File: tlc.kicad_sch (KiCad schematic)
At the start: 13 parts, among them U2 TL074, U3 TL074, U4 TLC7528

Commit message: started to work on power part
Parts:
- renumbered C1 to C7, C2 to C8, R1 to R19, R2 to R20, R3 to R21, R4 to R22, R5 to R23, R6 to R24, R7 to R25, R8 to R26, U2 to U3, U3 to U4, U4 to U5

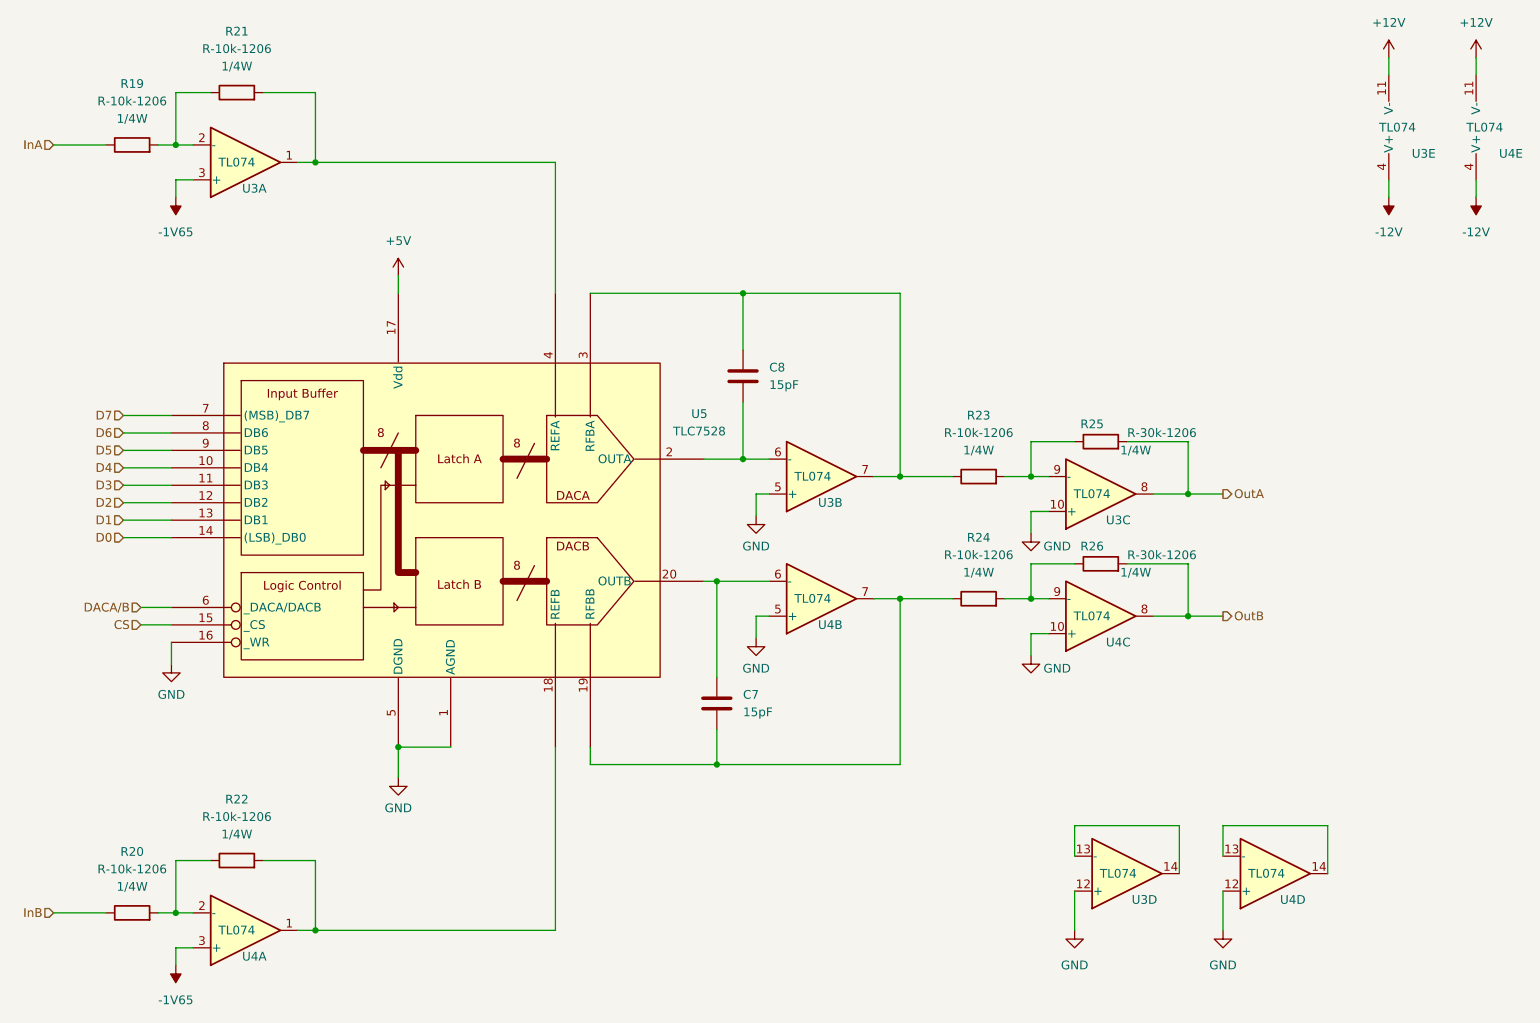
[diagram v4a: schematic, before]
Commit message: refactoring with global labels
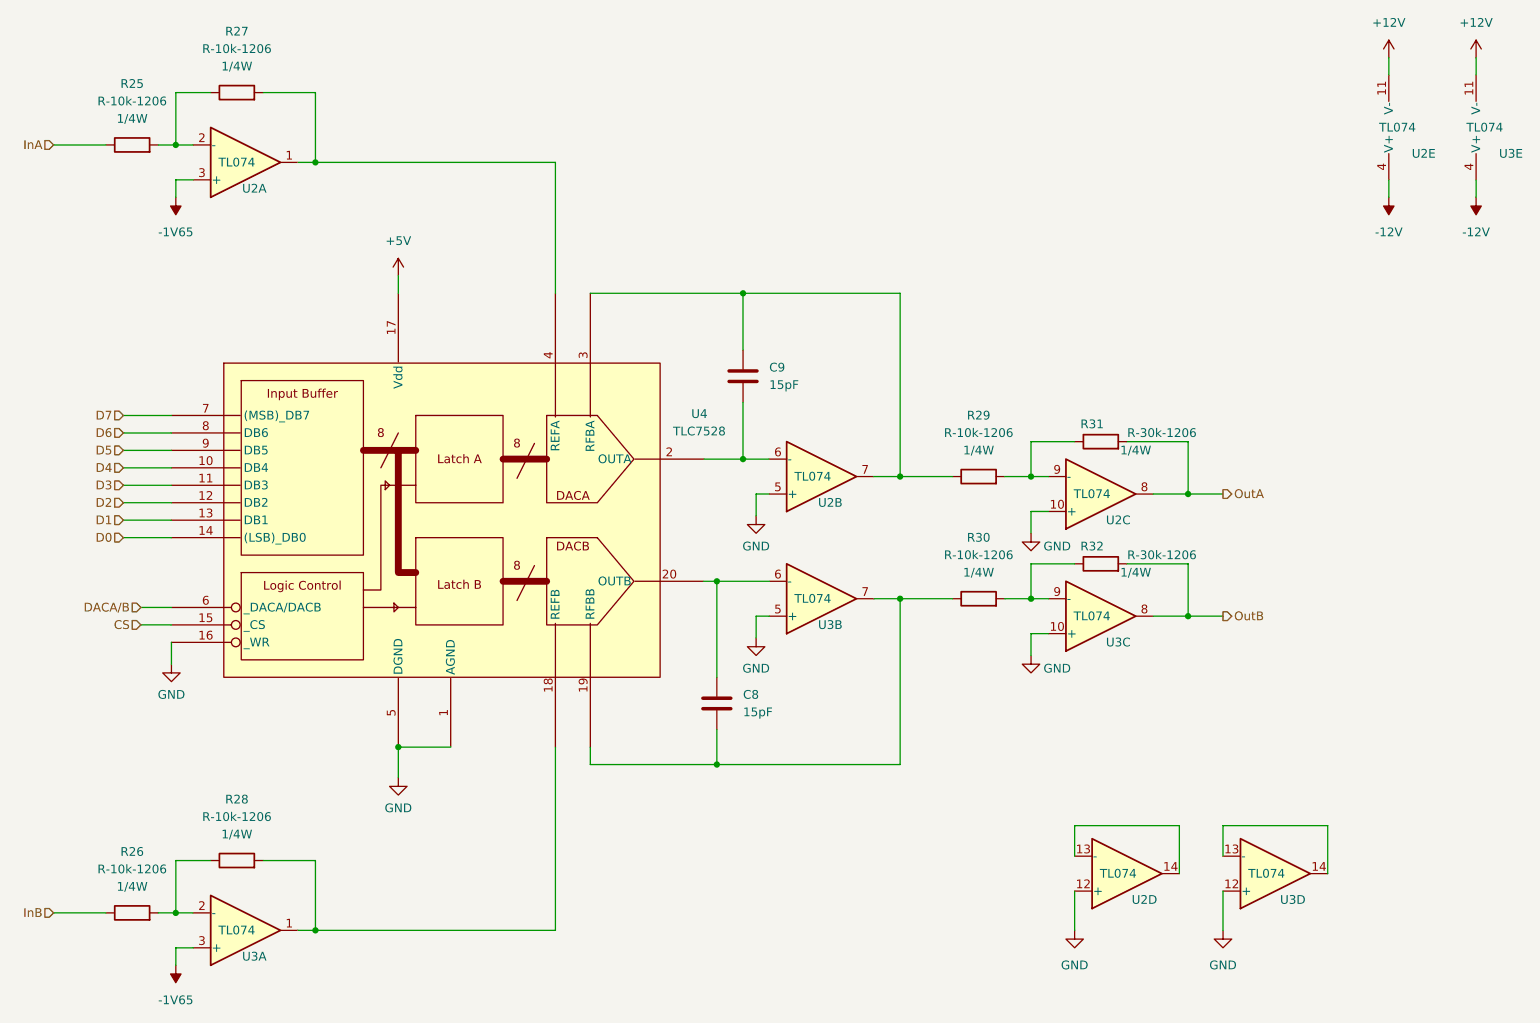
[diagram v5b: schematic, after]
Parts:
- renumbered C7 to C8, C8 to C9, R19 to R25, R20 to R26, R21 to R27, R22 to R28, R23 to R29, R24 to R30, R25 to R31, R26 to R32, U3 to U2, U4 to U3, U5 to U4

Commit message: cleaning into modules
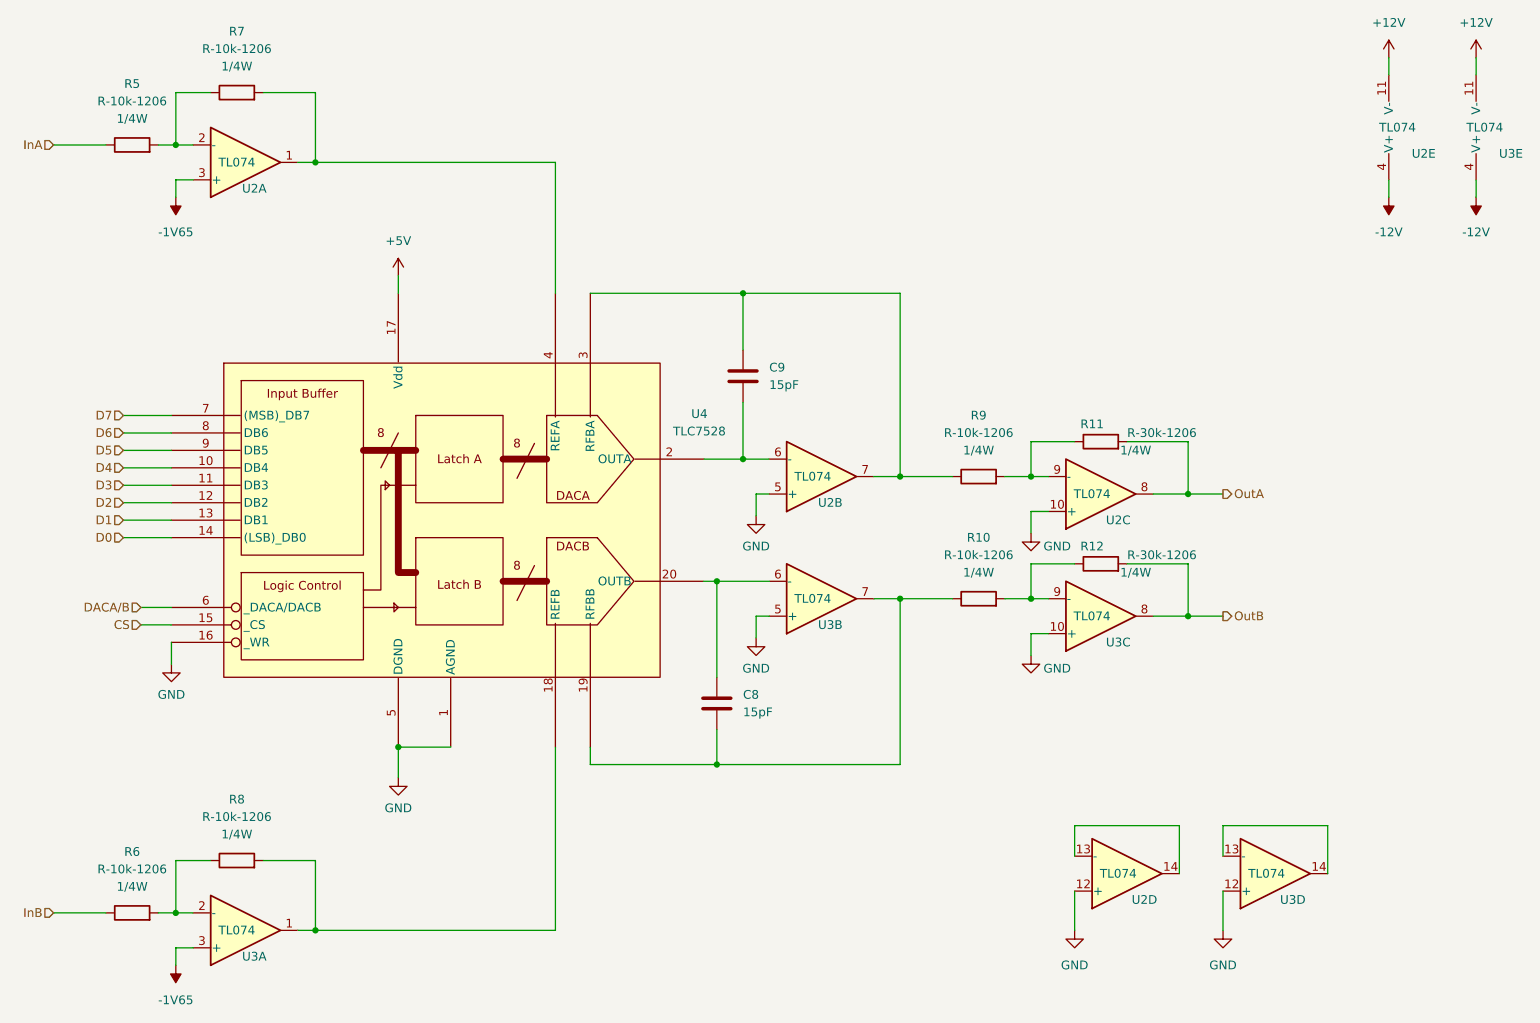
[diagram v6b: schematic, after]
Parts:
- renumbered R30 to R10, R31 to R11, R32 to R12, R25 to R5, R26 to R6, R27 to R7, R28 to R8, R29 to R9
